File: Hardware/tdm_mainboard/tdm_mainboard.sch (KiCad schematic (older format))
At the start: 67 parts, among them IC1 W25Q128JVSIQ, J1 Headphone, J2 LineIn, J3 Conn_02x06_Top_Bottom, J4 batteryConnection (jstph), U1 AP7313, U2 PAM8302AASCR, U3 SGTL5000, U4 Teensy4, U5 MCP73831T-2ACI_OT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

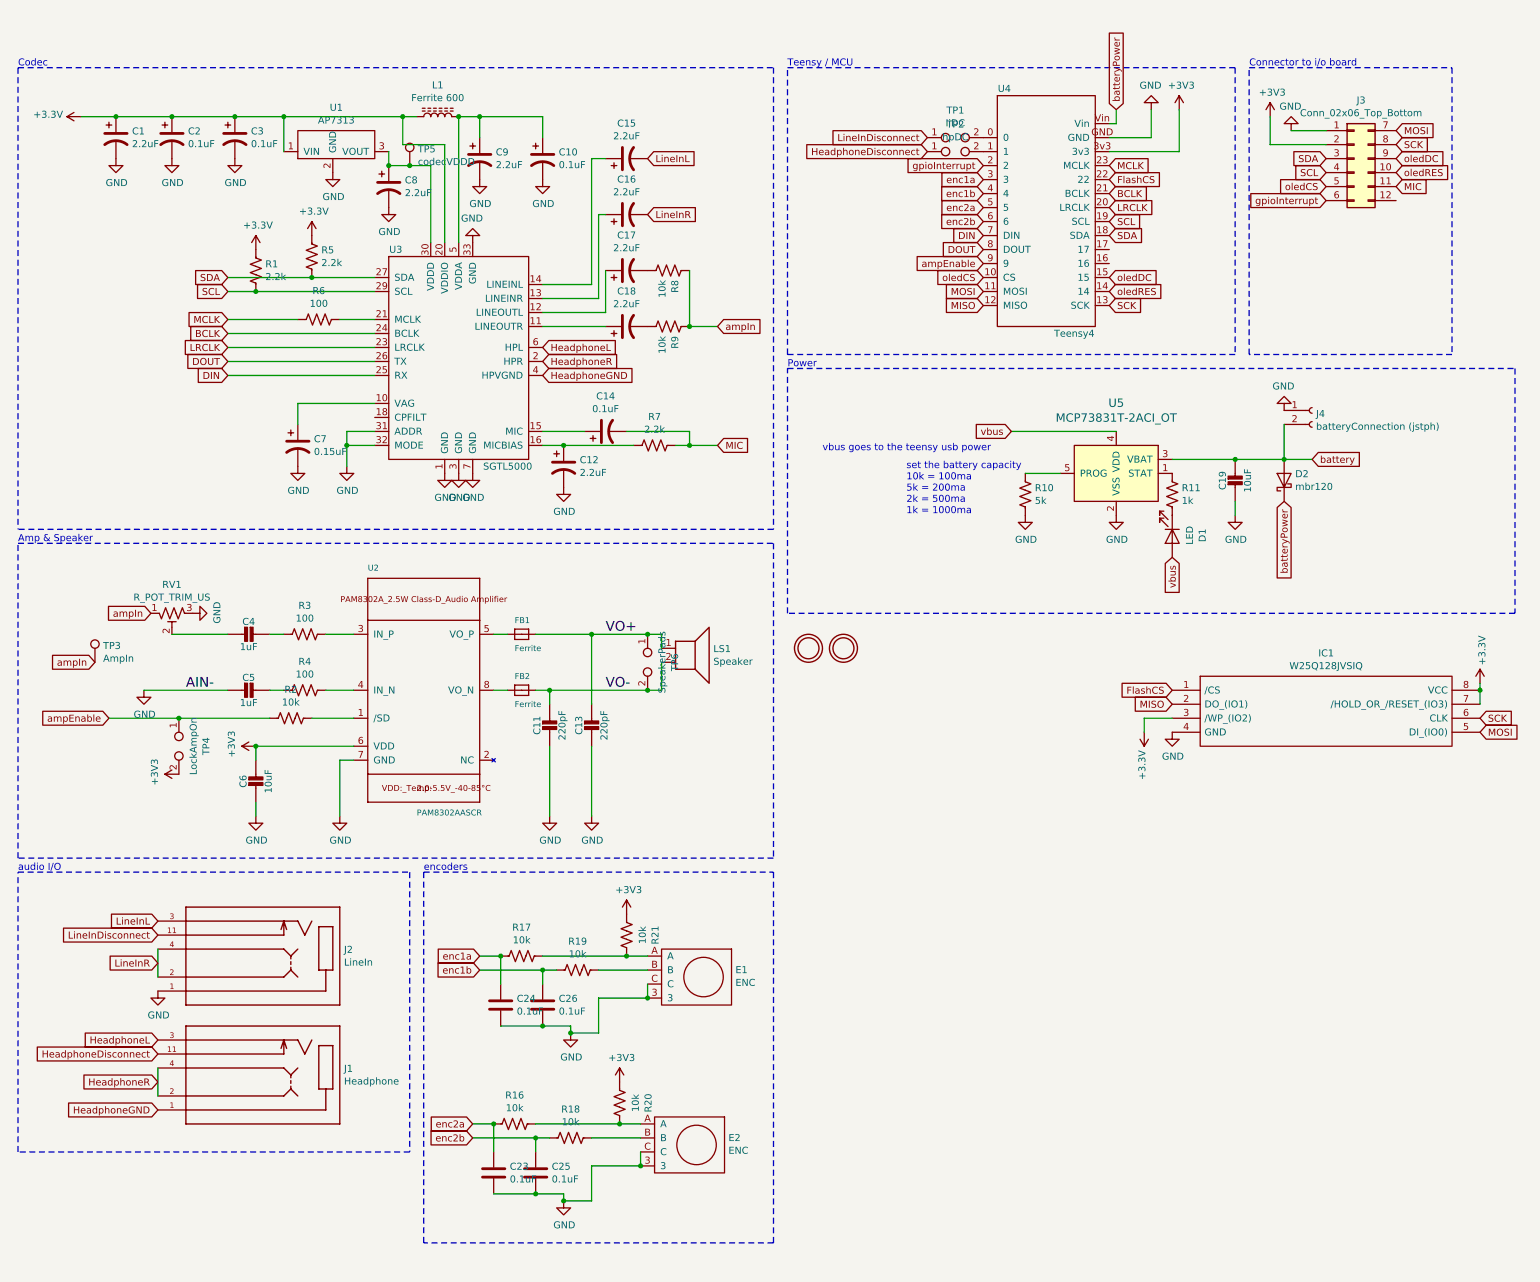
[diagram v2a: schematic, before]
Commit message: some changes to the backboad
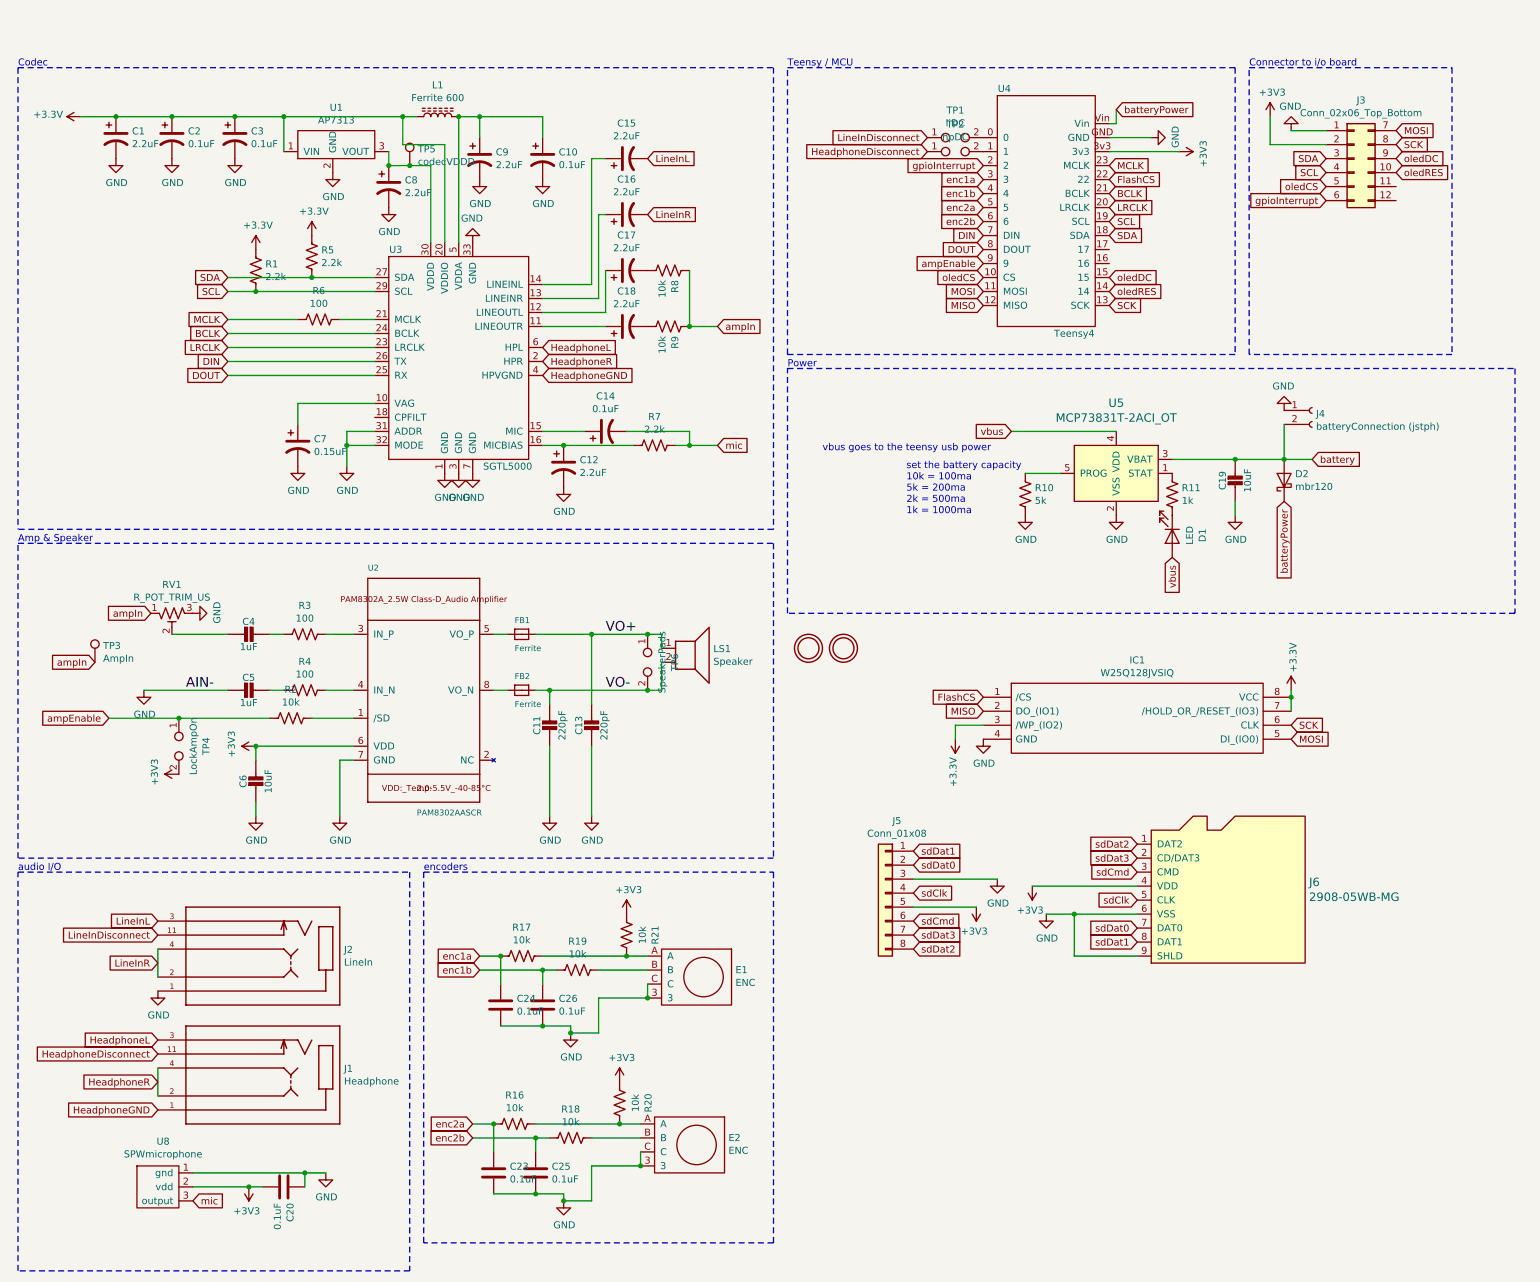
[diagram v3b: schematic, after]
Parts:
- added C20: 0.1uF, Capacitors_SMD:C_0603, symbol Device:C
- added J5: Conn_01x08, myLib:SFW8R-3STE1LF, symbol Connector_Generic:Conn_01x08
- added J6: 2908-05WB-MG, myLib:MOLEX_503182-1852_microsd, symbol dk_Memory-Connectors-PC-Card-Sockets:2908-05WB-MG
- added U8: SPWmicrophone, myLib:MIC_SPW2430HR5H-B, symbol customLibrary:SPWmicrophone
- D1: footprint (none) -> LEDs:LED_0603_HandSoldering
- D2: footprint (none) -> Diodes_SMD:D_SOD-123F
- J4: footprint (none) -> Connectors_JST:JST_PH_B2B-PH-K_02x2.00mm_Straight
- R10: footprint (none) -> Resistors_SMD:R_0603
- U5: footprint digikey-footprints:SOT-753 -> TO_SOT_Packages_SMD:SOT-23-5
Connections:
- net +3V3: now also C20.2, J5.5 (Pin_5), J6.4 (VDD), U8.2 (vdd)
- net DIN: now also U3.26 (TX); no longer U3.25 (RX)
- net DOUT: now also U3.25 (RX); no longer U3.26 (TX)
- net GND: now also C20.1, J5.3 (Pin_3), J6.6 (VSS), J6.9 (SHLD), U8.1 (gnd)
- net MIC renamed mic
- net mic: now also U8.3 (output); no longer J3.11 (Pin_11)
- new net sdClk: J5.4 (Pin_4), J6.5 (CLK)
- new net sdCmd: J5.6 (Pin_6), J6.3 (CMD)
- new net sdDat0: J5.2 (Pin_2), J6.7 (DAT0)
- new net sdDat1: J5.1 (Pin_1), J6.8 (DAT1)
- new net sdDat2: J5.8 (Pin_8), J6.1 (DAT2)
- new net sdDat3: J5.7 (Pin_7), J6.2 (CD/DAT3)
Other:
- moved on the sheet: IC1
